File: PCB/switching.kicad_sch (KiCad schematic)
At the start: 32 parts, among them J1 CURRENT, J2 24VAC, J3 3V3, U1 BD9G101G

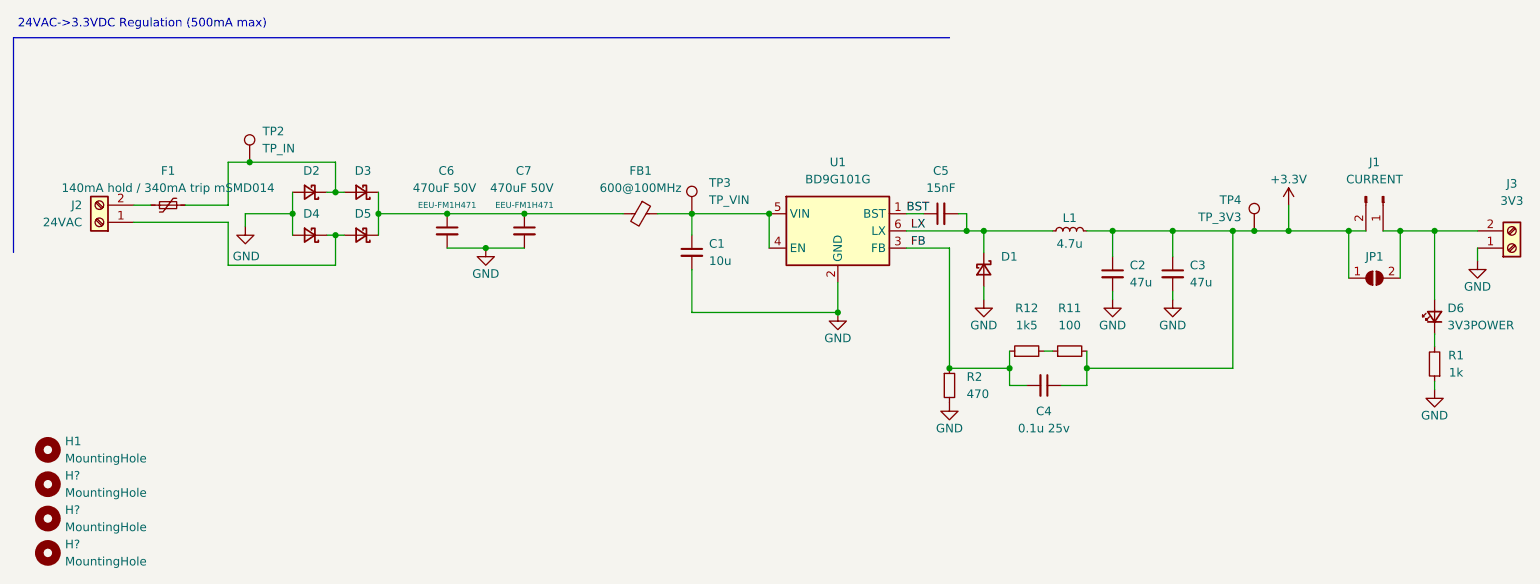
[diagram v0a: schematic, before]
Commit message: change barrier diode
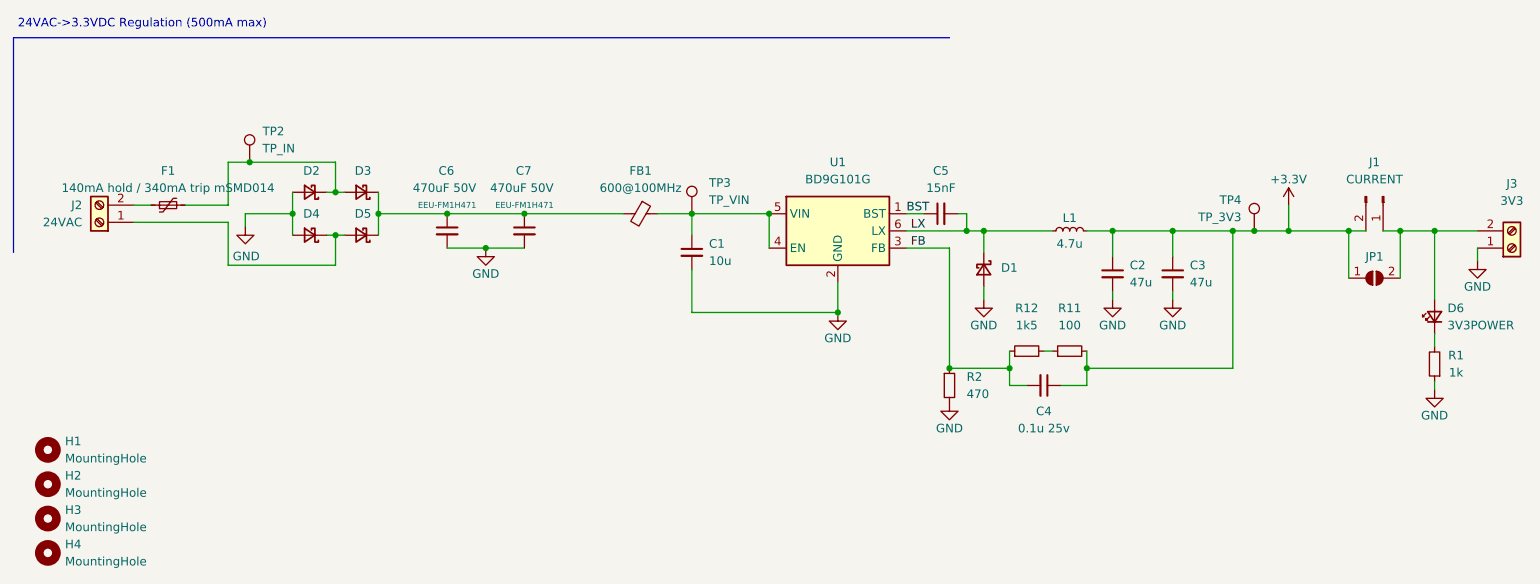
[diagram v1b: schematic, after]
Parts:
- D1: value SS36-E3/57T -> SS210; footprint Diode_SMD:D_SMC -> Diode_SMD:D_SMA; LCSC C35722 -> C14996
- gave numbers to parts that had none: 3
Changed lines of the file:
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@@
-    (pin "2")
-  )
-  (symbol (lib_id "Device:D_Schottky_Small") (at 158.75 52.07 270) (unit 1)
-    (in_bom yes) (on_board yes)
-    (property "Reference" "D1" (id 0) (at 161.29 50.165 90)
-      (effects (font (size 1.27 1.27)) (justify left))
-    )
-    (property "Value" "SS36-E3/57T" (id 1) (at 161.29 52.705 90)
-      (effects (font (size 1.27 1.27)) (justify left) hide)
-    )
-    (property "Footprint" "Diode_SMD:D_SMC" (id 2) (at 158.75 52.07 90)
-      (effects (font (size 1.27 1.27)) hide)
-    )
-    (property "Datasheet" "~" (id 3) (at 158.75 52.07 90)
-      (effects (font (size 1.27 1.27)) hide)
-    )
-    (property "LCSC" "C35722" (id 5) (at 158.75 52.07 0)
-      (effects (font (size 1.27 1.27)) hide)
-    )
-    (pin "1")
     (pin "2")
   )
@@
   (symbol (lib_id "Mechanical:MountingHole") (at 20.32 93.98 0) (unit 1)
     (in_bom yes) (on_board yes) (fields_autoplaced)
-    (property "Reference" "H?" (id 0) (at 22.86 92.7099 0)
+    (property "Reference" "H4" (id 0) (at 22.86 92.7099 0)
       (effects (font (size 1.27 1.27)) (justify left))
     )
@@
   (symbol (lib_id "Mechanical:MountingHole") (at 20.32 88.9 0) (unit 1)
     (in_bom yes) (on_board yes) (fields_autoplaced)
-    (property "Reference" "H?" (id 0) (at 22.86 87.6299 0)
+    (property "Reference" "H3" (id 0) (at 22.86 87.6299 0)
       (effects (font (size 1.27 1.27)) (justify left))
     )
@@
     )
     (property "LCSC" "a" (id 4) (at 216.535 53.34 0)
+      (effects (font (size 1.27 1.27)) hide)
+    )
+    (pin "1")
+    (pin "2")
+  )
+  (symbol (lib_id "Device:D_Schottky_Small") (at 158.75 52.07 270) (unit 1)
+    (in_bom yes) (on_board yes) (fields_autoplaced)
+    (property "Reference" "D1" (id 0) (at 161.29 51.8159 90)
+      (effects (font (size 1.27 1.27)) (justify left))
+    )
+    (property "Value" "SS210" (id 1) (at 154.94 51.816 0)
+      (effects (font (size 1.27 1.27)) hide)
+    )
+    (property "Footprint" "Diode_SMD:D_SMA" (id 2) (at 158.75 52.07 90)
+      (effects (font (size 1.27 1.27)) hide)
+    )
+    (property "Datasheet" "~" (id 3) (at 158.75 52.07 90)
+      (effects (font (size 1.27 1.27)) hide)
+    )
+    (property "LCSC" "C14996" (id 4) (at 158.75 52.07 0)
       (effects (font (size 1.27 1.27)) hide)
     )
@@
   (symbol (lib_id "Mechanical:MountingHole") (at 20.32 83.82 0) (unit 1)
     (in_bom yes) (on_board yes) (fields_autoplaced)
-    (property "Reference" "H?" (id 0) (at 22.86 82.5499 0)
+    (property "Reference" "H2" (id 0) (at 22.86 82.5499 0)
       (effects (font (size 1.27 1.27)) (justify left))
     )
@@
       (reference "C7") (unit 1) (value "470uF 50V") (footprint "Capacitor_THT:CP_Radial_D12.5mm_P5.00mm")
     )
-    (path "/39e94d92-ed8c-4aff-8253-65f327f02808"
-      (reference "D1") (unit 1) (value "SS36-E3/57T") (footprint "Diode_SMD:D_SMC")
+    (path "/c516da0c-07a3-4b49-be66-e1a315aafb1d"
+      (reference "D1") (unit 1) (value "SS210") (footprint "Diode_SMD:D_SMA")
     )
     (path "/41e17963-2e03-44a3-8fa3-0d47daa2d7d4"
@@
       (reference "H1") (unit 1) (value "MountingHole") (footprint "MountingHole:MountingHole_3.2mm_M3")
     )
+    (path "/f5af9b8d-0cd1-41cb-a08c-a217f0bb0ed9"
+      (reference "H2") (unit 1) (value "MountingHole") (footprint "MountingHole:MountingHole_3.2mm_M3")
+    )
+    (path "/bd1a938a-fe87-4c65-8209-1db88ae9ee01"
+      (reference "H3") (unit 1) (value "MountingHole") (footprint "MountingHole:MountingHole_3.2mm_M3")
+    )
     (path "/80e91cdd-8908-463b-8e21-99df87bea6cf"
-      (reference "H?") (unit 1) (value "MountingHole") (footprint "MountingHole:MountingHole_3.2mm_M3")
-    )
-    (path "/bd1a938a-fe87-4c65-8209-1db88ae9ee01"
-      (reference "H?") (unit 1) (value "MountingHole") (footprint "MountingHole:MountingHole_3.2mm_M3")
-    )
-    (path "/f5af9b8d-0cd1-41cb-a08c-a217f0bb0ed9"
-      (reference "H?") (unit 1) (value "MountingHole") (footprint "MountingHole:MountingHole_3.2mm_M3")
+      (reference "H4") (unit 1) (value "MountingHole") (footprint "MountingHole:MountingHole_3.2mm_M3")
     )
     (path "/0a5d104e-cf69-44ff-8471-dee821360840"

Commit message: convert to 2 layer
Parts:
- FB1: symbol Device:Ferrite_Bead_Small -> Device:FerriteBead_Small
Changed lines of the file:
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@@
     )
   )
-  (symbol (lib_id "Device:Ferrite_Bead_Small") (at 107.95 43.815 270) (unit 1)
+  (symbol (lib_id "Device:FerriteBead_Small") (at 107.95 43.815 270) (unit 1)
     (in_bom yes) (on_board yes) (fields_autoplaced)
     (property "Reference" "FB1" (id 0) (at 107.9881 37.465 90))

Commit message: add ground testpoints
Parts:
- added TP1, TP5, TP6: GND, TestPoint:TestPoint_Loop_D2.60mm_Drill1.6mm_Beaded, symbol Connector:TestPoint
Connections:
- net GND: now also TP1.1, TP5.1, TP6.1
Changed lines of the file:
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@@
   (junction (at 127 43.815) (diameter 0) (color 0 0 0 0)
   )
+  (junction (at 73.025 77.47) (diameter 0) (color 0 0 0 0)
+  )
   (junction (at 62.865 46.99) (diameter 0) (color 0 0 0 0)
   )
@@
     (stroke (width 0) (type default) (color 0 0 0 0))
   )
+  (wire (pts (xy 73.025 77.47) (xy 83.185 77.47))
+    (stroke (width 0) (type default) (color 0 0 0 0))
+  )
   (wire (pts (xy 225.425 46.355) (xy 231.775 46.355))
     (stroke (width 0) (type default) (color 0 0 0 0))
@@
   )
   (wire (pts (xy 61.595 40.64) (xy 62.865 40.64))
+    (stroke (width 0) (type default) (color 0 0 0 0))
+  )
+  (wire (pts (xy 60.96 77.47) (xy 73.025 77.47))
     (stroke (width 0) (type default) (color 0 0 0 0))
   )
@@
   (label "LX" (at 147.955 46.355 0)
     (effects (font (size 1.27 1.27)) (justify left bottom))
+  )
+  (symbol (lib_id "power:GND") (at 73.025 77.47 0) (unit 1)
+    (in_bom yes) (on_board yes)
+    (property "Reference" "#PWR0105" (id 0) (at 73.025 83.82 0)
+      (effects (font (size 1.27 1.27)) hide)
+    )
+    (property "Value" "GND" (id 1) (at 73.025 81.28 0))
+    (property "Footprint" "" (id 2) (at 73.025 77.47 0)
+      (effects (font (size 1.27 1.27)) hide)
+    )
+    (property "Datasheet" "" (id 3) (at 73.025 77.47 0)
+      (effects (font (size 1.27 1.27)) hide)
+    )
+    (pin "1")
   )
   (symbol (lib_id "Device:D_Schottky_Small") (at 66.675 46.99 180) (unit 1)
@@
     (pin "2")
   )
+  (symbol (lib_id "Connector:TestPoint") (at 60.96 77.47 0) (unit 1)
+    (in_bom yes) (on_board yes) (fields_autoplaced)
+    (property "Reference" "TP1" (id 0) (at 63.5 72.8979 0)
+      (effects (font (size 1.27 1.27)) (justify left))
+    )
+    (property "Value" "GND" (id 1) (at 63.5 75.4379 0)
+      (effects (font (size 1.27 1.27)) (justify left))
+    )
+    (property "Footprint" "TestPoint:TestPoint_Loop_D2.60mm_Drill1.6mm_Beaded" (id 2) (at 66.04 77.47 0)
+      (effects (font (size 1.27 1.27)) hide)
+    )
+    (property "Datasheet" "~" (id 3) (at 66.04 77.47 0)
+      (effects (font (size 1.27 1.27)) hide)
+    )
+    (property "LCSC" "a" (id 4) (at 60.96 77.47 0)
+      (effects (font (size 1.27 1.27)) hide)
+    )
+    (pin "1")
+  )
   (symbol (lib_id "Device:R_Small") (at 165.1 64.135 90) (unit 1)
     (in_bom yes) (on_board yes) (fields_autoplaced)
@@
     (pin "1")
   )
+  (symbol (lib_id "Connector:TestPoint") (at 83.185 77.47 0) (unit 1)
+    (in_bom yes) (on_board yes) (fields_autoplaced)
+    (property "Reference" "TP6" (id 0) (at 85.09 72.8979 0)
+      (effects (font (size 1.27 1.27)) (justify left))
+    )
+    (property "Value" "GND" (id 1) (at 85.09 75.4379 0)
+      (effects (font (size 1.27 1.27)) (justify left))
+    )
+    (property "Footprint" "TestPoint:TestPoint_Loop_D2.60mm_Drill1.6mm_Beaded" (id 2) (at 88.265 77.47 0)
+      (effects (font (size 1.27 1.27)) hide)
+    )
+    (property "Datasheet" "~" (id 3) (at 88.265 77.47 0)
+      (effects (font (size 1.27 1.27)) hide)
+    )
+    (property "LCSC" "a" (id 4) (at 83.185 77.47 0)
+      (effects (font (size 1.27 1.27)) hide)
+    )
+    (pin "1")
+  )
   (symbol (lib_id "Device:D_Schottky_Small") (at 66.675 40.64 180) (unit 1)
     (in_bom yes) (on_board yes) (fields_autoplaced)
@@
     (pin "2")
   )
+  (symbol (lib_id "Connector:TestPoint") (at 73.025 77.47 0) (unit 1)
+    (in_bom yes) (on_board yes) (fields_autoplaced)
+    (property "Reference" "TP5" (id 0) (at 74.93 72.8979 0)
+      (effects (font (size 1.27 1.27)) (justify left))
+    )
+    (property "Value" "GND" (id 1) (at 74.93 75.4379 0)
+      (effects (font (size 1.27 1.27)) (justify left))
+    )
+    (property "Footprint" "TestPoint:TestPoint_Loop_D2.60mm_Drill1.6mm_Beaded" (id 2) (at 78.105 77.47 0)
+      (effects (font (size 1.27 1.27)) hide)
+    )
+    (property "Datasheet" "~" (id 3) (at 78.105 77.47 0)
+      (effects (font (size 1.27 1.27)) hide)
+    )
+    (property "LCSC" "a" (id 4) (at 73.025 77.47 0)
+      (effects (font (size 1.27 1.27)) hide)
+    )
+    (pin "1")
+  )
   (sheet_instances
     (path "/" (page "1"))
@@
       (reference "#PWR0104") (unit 1) (value "GND") (footprint "")
     )
+    (path "/05e8cbc5-07d6-469c-baa6-157f49fb966a"
+      (reference "#PWR0105") (unit 1) (value "GND") (footprint "")
+    )
     (path "/86b15643-f0f8-442e-a3da-e7c1cf895675"
       (reference "#PWR0106") (unit 1) (value "GND") (footprint "")
@@
       (reference "R12") (unit 1) (value "1k5") (footprint "Resistor_SMD:R_0402_1005Metric")
     )
+    (path "/4cf91f04-b74a-446b-99cd-d85528cbad0a"
+      (reference "TP1") (unit 1) (value "GND") (footprint "TestPoint:TestPoint_Loop_D2.60mm_Drill1.6mm_Beaded")
+    )
     (path "/8e6179e7-4f78-47ee-a01f-0f2835460f39"
       (reference "TP2") (unit 1) (value "TP_IN") (footprint "TestPoint:TestPoint_Loop_D2.60mm_Drill1.6mm_Beaded")
@@
       (reference "TP4") (unit 1) (value "TP_3V3") (footprint "TestPoint:TestPoint_Loop_D2.60mm_Drill1.6mm_Beaded")
     )
+    (path "/fe0d8834-f0dd-4322-9282-52ab3c141d80"
+      (reference "TP5") (unit 1) (value "GND") (footprint "TestPoint:TestPoint_Loop_D2.60mm_Drill1.6mm_Beaded")
+    )
+    (path "/8f9ec488-8c95-45ca-b576-efb79e985c8e"
+      (reference "TP6") (unit 1) (value "GND") (footprint "TestPoint:TestPoint_Loop_D2.60mm_Drill1.6mm_Beaded")
+    )
     (path "/1c4d7e84-b465-4e8a-b1c9-e9391f0f94a9"

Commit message: smaller and smd only to use in designs
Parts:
- removed C7: 470uF 50V, Capacitor_THT:CP_Radial_D12.5mm_P5.00mm, symbol Device:C_Small
- removed D6: 3V3POWER, LED_SMD:LED_0603_1608Metric, symbol Device:LED_Small
- removed J1: CURRENT, Connector_PinHeader_2.54mm:PinHeader_1x02_P2.54mm_Vertical, symbol Connector:Conn_01x02_Male
- removed JP1: CURRENTJUMP, Jumper:SolderJumper-2_P1.3mm_Open_RoundedPad1.0x1.5mm, symbol Jumper:SolderJumper_2_Open
- removed R1: 1k, Resistor_SMD:R_0603_1608Metric, symbol Device:R_Small
- removed TP1, TP5, TP6: GND, TestPoint:TestPoint_Loop_D2.60mm_Drill1.6mm_Beaded, symbol Connector:TestPoint
- removed TP2: TP_IN, TestPoint:TestPoint_Loop_D2.60mm_Drill1.6mm_Beaded, symbol Connector:TestPoint
- removed TP3: TP_VIN, TestPoint:TestPoint_Loop_D2.60mm_Drill1.6mm_Beaded, symbol Connector:TestPoint
- removed TP4: TP_3V3, TestPoint:TestPoint_Loop_D2.60mm_Drill1.6mm_Beaded, symbol Connector:TestPoint
- C6: footprint Capacitor_THT:CP_Radial_D12.5mm_P5.00mm -> Capacitor_SMD:CP_Elec_10x10; LCSC DNP -> C125977; Part EEU-FM1H471 -> (none)
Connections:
- net +3.3V: now also J3.2 (Pin_2)
- net BST: no longer names the net of C5.1, U1.1 (BST)
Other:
- note added: "Confirm fuse sizing depending on input voltage. (eg. 5VDC need bigger fuse)"
- moved on the sheet: C1, C2, C3, C4, C5, C6, D1, D2, D3, D4, D5, F1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
